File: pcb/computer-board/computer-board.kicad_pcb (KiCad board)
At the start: 4 copper layers, 100 x 50 mm, 100 parts, among them J1 Conn_01x02_Male, J2 Conn_01x02_Male, J3 Conn_02x03_Counter_Clockwise, J4 Conn_02x20_Odd_Even, J5 Conn_01x04_Male, J6 Conn_01x02, SW1 SW_Push, U1 TLV73333PDBV, U10 74LVC16374ADGG,112, U11 74LVC16374ADGG,112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

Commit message: Version 1.0
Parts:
- added REF**: WEEE-Logo_4.2x6mm_SilkScreen, Symbol:WEEE-Logo_4.2x6mm_SilkScreen, B.Cu at (126.0, 122.0)
- added REF**: ESD-Logo_6.6x6mm_SilkScreen, Symbol:ESD-Logo_6.6x6mm_SilkScreen, B.Cu at (119.0, 122.0)

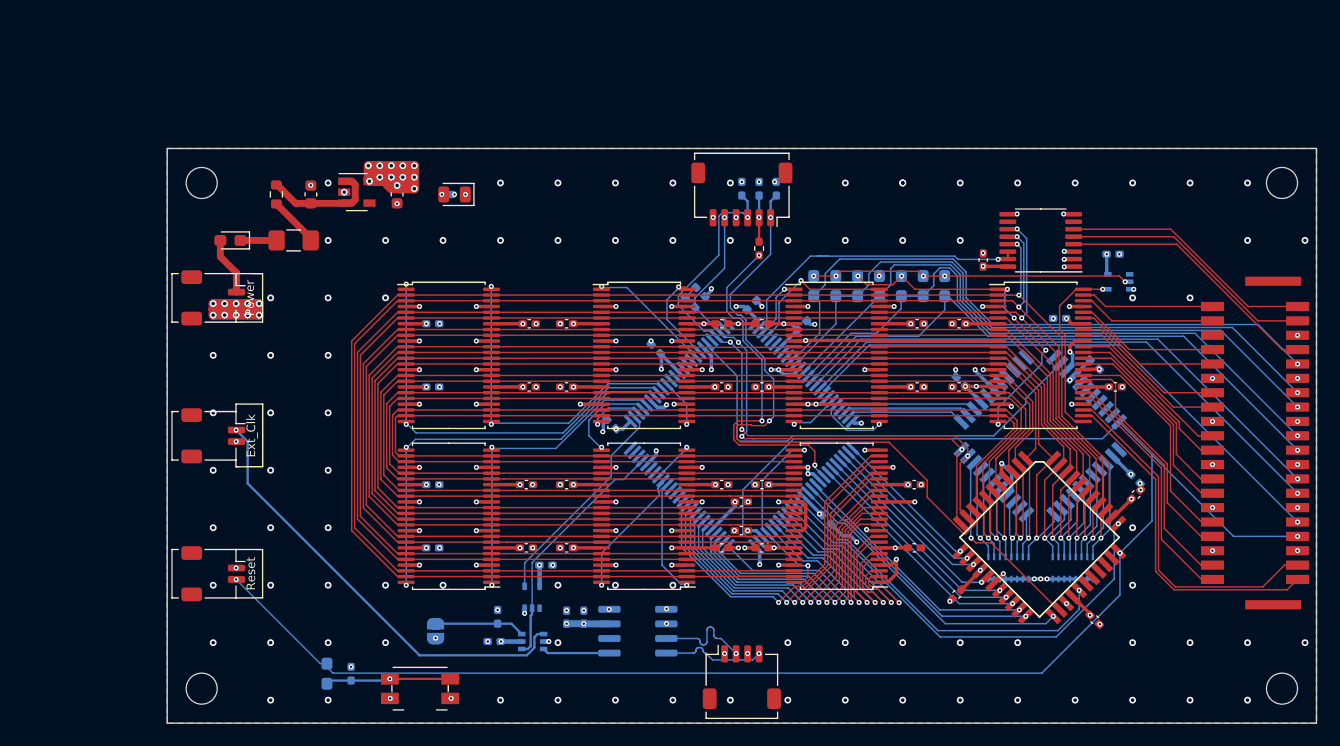
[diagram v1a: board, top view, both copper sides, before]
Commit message: Remove and change connectors for a mezzanine one
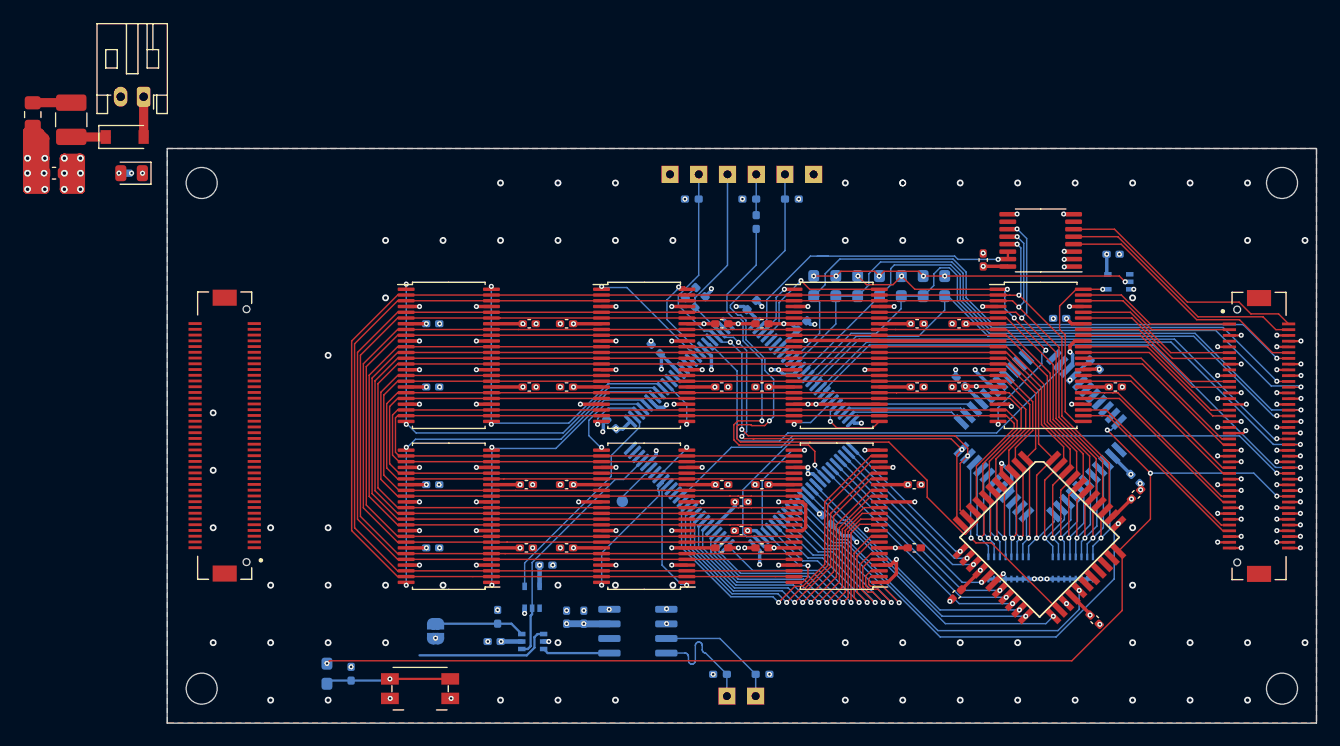
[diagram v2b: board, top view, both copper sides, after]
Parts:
- removed C2: 10u, Capacitor_SMD:C_0603_1608Metric
- removed J3: Conn_02x03_Counter_Clockwise, Connector_Molex:Molex_Pico-Clasp_202396-0607_1x06-1MP_P1.00mm_Horizontal
- removed J4: Conn_02x20_Odd_Even, Connector_Molex:Micro-Lock-Plus-02x20
- removed J5: Conn_01x04_Male, Connector_Molex:Molex_Pico-Clasp_202396-0407_1x04-1MP_P1.00mm_Horizontal
- removed J6: Conn_01x02, Connector_Molex:Molex_Pico-Clasp_202396-0207_1x02-1MP_P1.00mm_Horizontal
- removed REF**: WEEE-Logo_4.2x6mm_SilkScreen, Symbol:WEEE-Logo_4.2x6mm_SilkScreen
- removed REF**: ESD-Logo_6.6x6mm_SilkScreen, Symbol:ESD-Logo_6.6x6mm_SilkScreen
- removed U1: TLV73333PDBV, Package_TO_SOT_SMD:SOT-23-5
- added J7: Conn_02x40_Odd_Even, Connector_Hirose:HRS_DF17(2.0)-80DP-0.5V(57), F.Cu at (131.0, 102.0)
- added R10: 10k, Resistor_SMD:R_0402_1005Metric_Pad0.72x0.64mm_HandSolder, B.Cu at (87.8, 122.8)
- added R9: 10k, Resistor_SMD:R_0402_1005Metric_Pad0.72x0.64mm_HandSolder, B.Cu at (84.1, 122.8)
- added TP1: TestPoint_Small, TestPoint:TestPoint_Pad_D1.0mm, B.Cu at (75.6, 107.7)
- added TP10: TestPoint_Small, TestPoint:TestPoint_THTPad_1.5x1.5mm_Drill0.7mm, F.Cu at (87.2, 124.7)
- added TP2: TestPoint_Small, TestPoint:TestPoint_THTPad_1.5x1.5mm_Drill0.7mm, F.Cu at (79.8, 79.2)
- added TP3: TestPoint_Small, TestPoint:TestPoint_THTPad_1.5x1.5mm_Drill0.7mm, F.Cu at (89.8, 79.2)
- added TP4: TestPoint_Small, TestPoint:TestPoint_THTPad_1.5x1.5mm_Drill0.7mm, F.Cu at (87.2, 79.2)
- added TP5: TestPoint_Small, TestPoint:TestPoint_THTPad_1.5x1.5mm_Drill0.7mm, F.Cu at (84.8, 79.2)
- added TP6: TestPoint_Small, TestPoint:TestPoint_THTPad_1.5x1.5mm_Drill0.7mm, F.Cu at (82.2, 79.2)
- added TP7: TestPoint_Small, TestPoint:TestPoint_THTPad_1.5x1.5mm_Drill0.7mm, F.Cu at (92.2, 79.2)
- added TP8: TestPoint_Small, TestPoint:TestPoint_THTPad_1.5x1.5mm_Drill0.7mm, F.Cu at (84.7, 124.7)
- C1: footprint Capacitor_SMD:C_0603_1608Metric -> Capacitor_SMD:C_0603_1608Metric_Pad1.08x0.95mm_HandSolder
- D1: value D_Schottky_Small -> Schottky 2A; footprint Diode_SMD:D_0603_1608Metric_Pad1.05x0.95mm_HandSolder -> Diode_SMD:D_SOD-123
- F1: value 250mA -> A déterminer; footprint Fuse:Fuse_1206_3216Metric_Pad1.42x1.75mm_HandSolder -> Fuse:Fuse_1210_3225Metric_Pad1.42x2.65mm_HandSolder
- FB1: footprint Resistor_SMD:R_0603_1608Metric -> Inductor_SMD:L_0805_2012Metric_Pad1.15x1.40mm_HandSolder
- J1: footprint Connector_Molex:Molex_Pico-Clasp_202396-0207_1x02-1MP_P1.00mm_Horizontal -> Connector_JST:JST_PH_S2B-PH-K_1x02_P2.00mm_Horizontal
- J2: value Conn_01x02_Male -> Conn_02x40_Odd_Even; footprint Connector_Molex:Molex_Pico-Clasp_202396-0207_1x02-1MP_P1.00mm_Horizontal -> Connector_Hirose:HRS_DF17(2.0)-80DP-0.5V(57)
- R5: moved to B.Cu
- moved D10 28.2 mm to (32.9, 79.2)
- moved R8 28.2 mm to (33.3, 79.2)
- moved C1 22.4 mm to (26.1, 79.2), turned to 0 degrees
- moved FB1 22.3 mm to (24.3, 74.0), turned to 90 degrees
- moved F1 22.0 mm to (27.6, 74.5), turned to 270 degrees
- moved J1 18.5 mm to (34.0, 72.5), turned to 180 degrees
- moved D1 12.9 mm to (32.3, 76.0), turned to 0 degrees
- moved J2 12.0 mm to (41.0, 102.0), turned to 90 degrees
- moved R4 4.45 mm to (81.6, 81.4), turned to 0 degrees
- moved R5 2.31 mm to (87.2, 83.4)
- moved R2 1.63 mm to (90.4, 81.4), turned to 180 degrees
- moved R3 1.24 mm to (86.6, 81.4), turned to 0 degrees
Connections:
- net Net-(J3-Pad2) renamed /TDO_Conn
- C1 pad 1: Net-(C1-Pad1) -> +3V3
- FB1 pad 1: Net-(C1-Pad1) -> +3V3
- J2 pad 2: /RESET -> GND
- U14 pad 13: Net-(U14-Pad13) -> /MEM_READY
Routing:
- net /MEM_READY: track 0.00 -> 56.6 mm, vias 0 -> 1
- net GND: track 162.3 -> 205.1 mm, vias 238 -> 231
- net /RESET: track 156.9 -> 115.9 mm, vias 3 -> 4
- net EXT_CLK: track 38.3 -> 12.1 mm, vias 1 -> 0
- net +3V3: track 146.5 -> 161.3 mm, vias 70 -> 78
- net /IO/IO15: track 30.6 -> 16.9 mm
- net /IO/IO16: track 30.0 -> 16.9 mm
- net Net-(C1-Pad1): track 10.1 -> 0.00 mm
- net /IO/IO14: track 21.4 -> 16.4 mm
- net /IO/IO12: track 20.4 -> 16.0 mm
- net /IO/IO13: track 20.7 -> 16.4 mm
- net Net-(TP1-Pad1): track 0.00 -> 3.88 mm
- net /TCK: track 49.2 -> 53.1 mm, vias 4 -> 3
- net /IO/IO11: track 19.8 -> 16.0 mm
- net /IO/IO1: track 11.7 -> 14.4 mm
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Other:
- board text removed: "Ext_Clk"
- board text removed: "Power"
- board text removed: "Reset"

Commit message: Revision 2 is ready
Need to wait for the testing of rev 1 before ordering
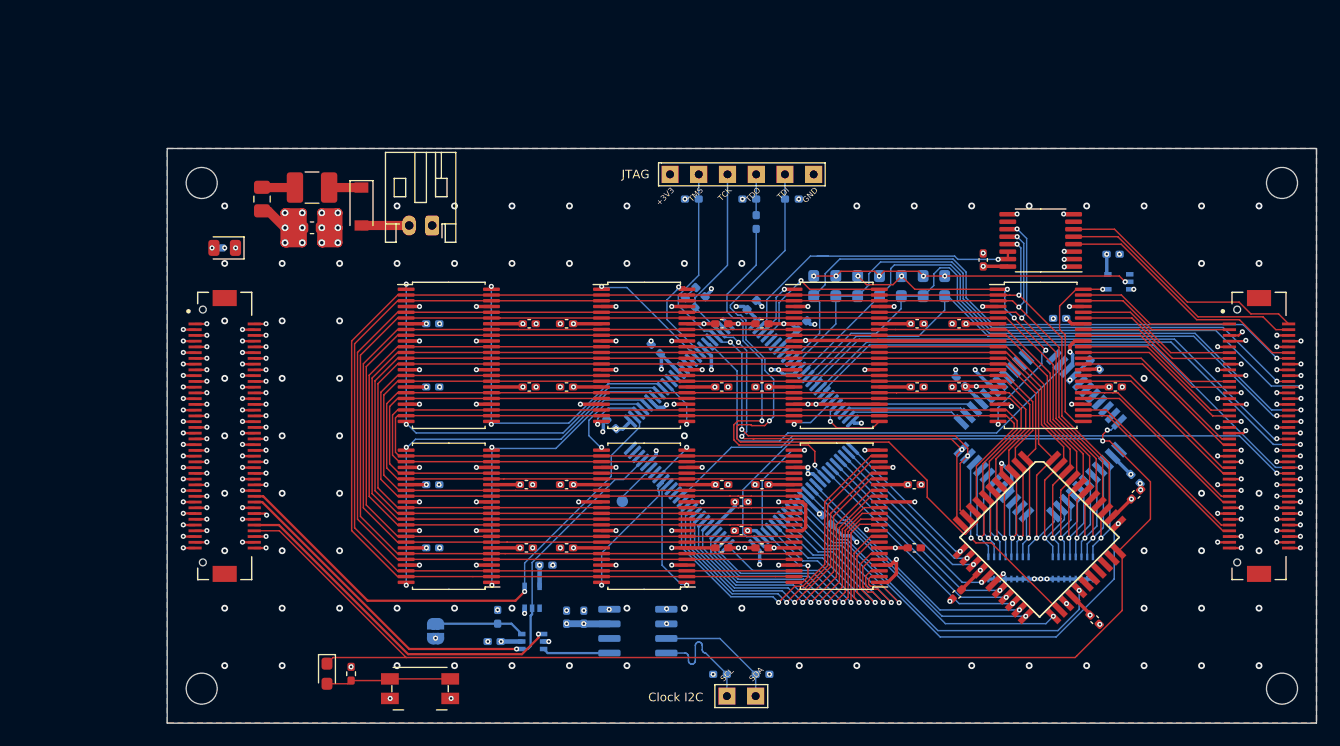
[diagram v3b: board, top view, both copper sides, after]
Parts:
- added REF**: WEEE-Logo_5.6x8mm_SilkScreen, Symbol:WEEE-Logo_5.6x8mm_SilkScreen, B.Cu at (116.0, 121.0)
- added REF**: ESD-Logo_8.9x8mm_SilkScreen, Symbol:ESD-Logo_8.9x8mm_SilkScreen, B.Cu at (125.0, 121.0)
- D2, R1: moved to F.Cu
- moved J1 27.5 mm to (59.0, 83.7)
- moved C1 22.9 mm to (48.6, 83.9)
- moved F1 21.8 mm to (48.6, 80.4), turned to 0 degrees
- moved D1 21.5 mm to (52.9, 82.0), turned to 270 degrees
- moved FB1 21.3 mm to (44.2, 81.4)
- moved D10 10.4 mm to (41.0, 85.7)
- moved R8 10.4 mm to (41.4, 85.7)
- turned J2 to 270 degrees
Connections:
- J1 pad 1: VCC -> GND
- J1 pad 2: GND -> VCC
- J2 pad 62: GND -> /CLK_I
- J2 pad 64: GND -> /CLK
- J2 pad 72: GND -> /EXT_CLK
- J2 pad 74: GND -> /RESET
- J7 pad 62: /RESET -> GND
- U14 pad 22: /Clocks/CLK -> /CLK
- U14 pad 27: /Clocks/CLK_I -> /CLK_I
- U17 pad 1: EXT_CLK -> /EXT_CLK
- U17 pad 4: /Clocks/CLK -> /CLK
- U18 pad 2: /Clocks/CLK -> /CLK
- U18 pad 4: /Clocks/CLK_I -> /CLK_I
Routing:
- net GND: track 205.1 -> 265.4 mm, vias 231 -> 301
- net /CLK: track 0.00 -> 50.1 mm, vias 0 -> 1
- net /CLK_I: track 0.00 -> 47.1 mm, vias 0 -> 1
- net /RESET: track 115.9 -> 148.9 mm, vias 4 -> 2
- net /EXT_CLK: track 0.00 -> 30.7 mm, vias 0 -> 1
- net /Clocks/CLK: track 21.5 -> 0.00 mm
- net /Clocks/CLK_I: track 19.0 -> 0.00 mm
- net EXT_CLK: track 12.1 -> 0.00 mm
- net +3V3: track 161.3 -> 167.1 mm, vias 78 -> 96
- net VCC: track 3.50 -> 4.15 mm
- net Net-(D2-Pad2): track 10.8 -> 10.9 mm, vias 1 -> 0
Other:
- board text added: "+3V3"
- board text added: "Clock I2C"
- board text added: "Compute Module"
- board text added: "GND"
- board text added: "JTAG"
- board text added: "SCL"
- board text added: "SDA"
- board text added: "TCK"
- board text added: "TDI"
- board text added: "TDO"
- board text added: "TMS"
- board text added: "— Rev 2 —"

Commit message: added pulldowns on diode logic
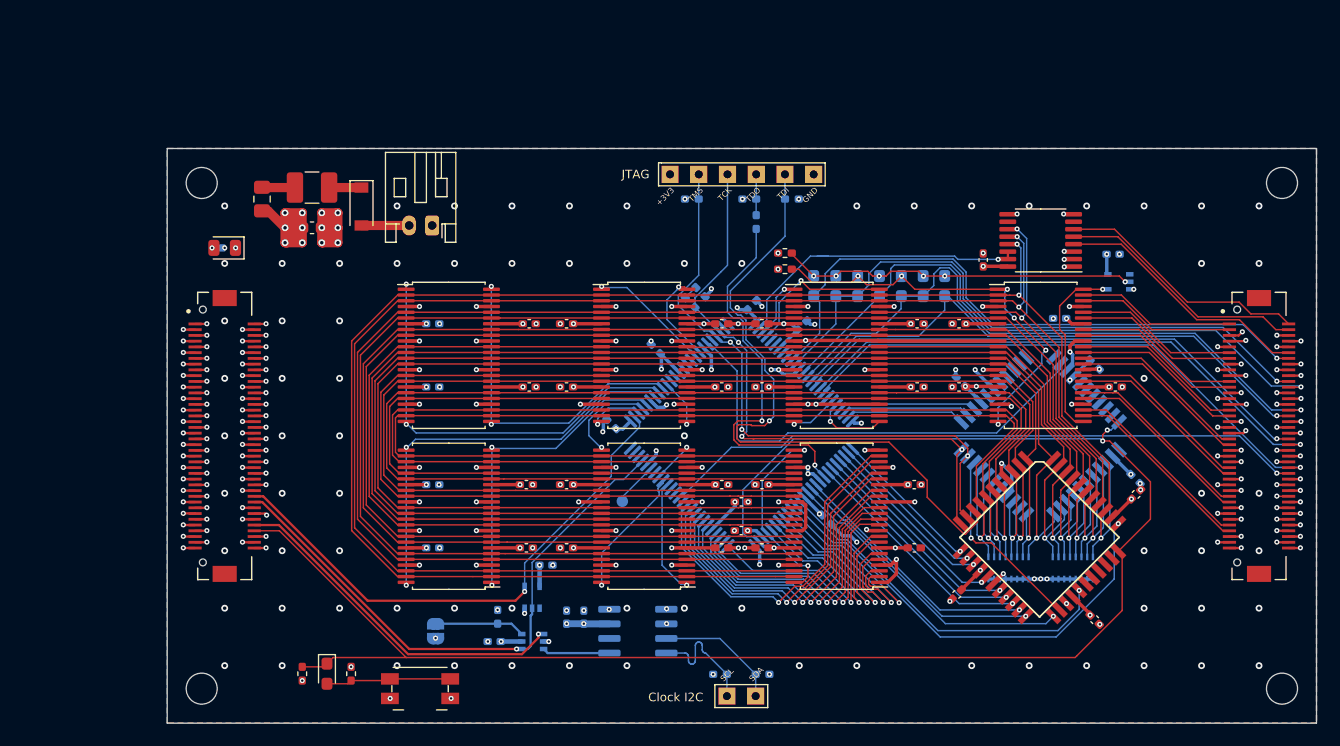
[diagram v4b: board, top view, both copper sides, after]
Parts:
- removed REF**: WEEE-Logo_5.6x8mm_SilkScreen, Symbol:WEEE-Logo_5.6x8mm_SilkScreen
- removed REF**: ESD-Logo_8.9x8mm_SilkScreen, Symbol:ESD-Logo_8.9x8mm_SilkScreen
- added R11: 10k, Resistor_SMD:R_0402_1005Metric_Pad0.72x0.64mm_HandSolder, F.Cu at (47.8, 122.7)
- added R12: 10k, Resistor_SMD:R_0402_1005Metric_Pad0.72x0.64mm_HandSolder, F.Cu at (89.8, 87.5)
- added R13: 10k, Resistor_SMD:R_0402_1005Metric_Pad0.72x0.64mm_HandSolder, F.Cu at (89.8, 86.1)
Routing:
- net Net-(D4-Pad1): track 29.4 -> 35.9 mm
- net Net-(D3-Pad1): track 28.4 -> 31.3 mm
- net /RESET: track 148.9 -> 151.1 mm
- net GND: vias 301 -> 304
